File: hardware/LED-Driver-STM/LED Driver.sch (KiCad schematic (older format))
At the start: 3 parts, among them Q1 2N7002

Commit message: Finished Routing V1
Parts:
- D4: LCSC (none) -> C2286
- Q1: LCSC (none) -> C8545
- R9: LCSC (none) -> C25133
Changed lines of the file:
@@
 $Descr A4 11693 8268
 encoding utf-8
-Sheet 3 21
+Sheet 8 21
 Title ""
 Date ""
@@
 AR Path="/5F90BCB5/5F71D34C" Ref="R26"  Part="1"
 AR Path="/5F90BCB8/5F71D34C" Ref="R27"  Part="1"
-F 0 "R9" H 5368 3196 50  0000 L CNN
+F 0 "R14" H 5368 3196 50  0000 L CNN
 F 1 "75" H 5368 3105 50  0000 L CNN
 F 2 "Resistor_SMD:R_0402_1005Metric" H 5300 3150 50  0001 C CNN
 F 3 "~" H 5300 3150 50  0001 C CNN
 F 4 "C25133" H 5300 3150 50  0001 C CNN "LCSC Part #"
+F 5 "C25133" H 5300 3150 50  0001 C CNN "LCSC"
 	1    5300 3150
 	1    0    0    -1
@@
 AR Path="/5F90BCB5/5F71D352" Ref="D21"  Part="1"
 AR Path="/5F90BCB8/5F71D352" Ref="D22"  Part="1"
-F 0 "D4" V 5339 2683 50  0000 R CNN
+F 0 "D9" V 5339 2683 50  0000 R CNN
 F 1 "LED" V 5248 2683 50  0000 R CNN
 F 2 "LED_SMD:LED_0603_1608Metric_Castellated" H 5300 2800 50  0001 C CNN
 F 3 "~" H 5300 2800 50  0001 C CNN
 F 4 "C2286" H 5300 2800 50  0001 C CNN "LCSC Part #"
+F 5 "C2286" H 5300 2800 50  0001 C CNN "LCSC"
 	1    5300 2800
 	0    -1   -1   0
@@
 AR Path="/5F90BCB5/5F71EA4B" Ref="Q19"  Part="1"
 AR Path="/5F90BCB8/5F71EA4B" Ref="Q20"  Part="1"
-F 0 "Q2" H 5404 3596 50  0000 L CNN
+F 0 "Q7" H 5404 3596 50  0000 L CNN
 F 1 "2N7002" H 5404 3505 50  0000 L CNN
 F 2 "Package_TO_SOT_SMD:SOT-23" H 5400 3475 50  0001 L CIN
 F 3 "https://datasheet.lcsc.com/szlcsc/Changjiang-Electronics-Tech-CJ-2N7002_C8545.pdf" H 5200 3550 50  0001 L CNN
 F 4 "C8545" H 5200 3550 50  0001 C CNN "LCSC Part #"
+F 5 "C8545" H 5200 3550 50  0001 C CNN "LCSC"
 	1    5200 3550
 	1    0    0    -1

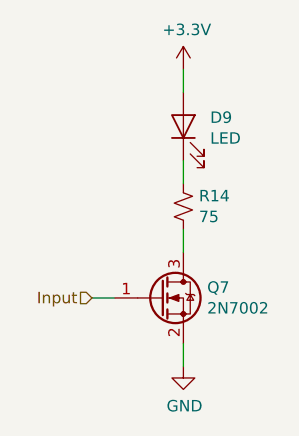
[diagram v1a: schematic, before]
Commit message: Latest board layout
This is the board that was purchased
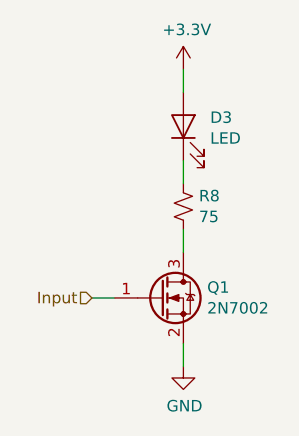
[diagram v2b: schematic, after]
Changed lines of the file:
@@
 $Descr A4 11693 8268
 encoding utf-8
-Sheet 8 21
+Sheet 2 21
 Title ""
 Date ""
@@
 AR Path="/5F90BCB5/5F71D34C" Ref="R26"  Part="1"
 AR Path="/5F90BCB8/5F71D34C" Ref="R27"  Part="1"
-F 0 "R14" H 5368 3196 50  0000 L CNN
+F 0 "R8" H 5368 3196 50  0000 L CNN
 F 1 "75" H 5368 3105 50  0000 L CNN
 F 2 "Resistor_SMD:R_0402_1005Metric" H 5300 3150 50  0001 C CNN
@@
 AR Path="/5F90BCB5/5F71D352" Ref="D21"  Part="1"
 AR Path="/5F90BCB8/5F71D352" Ref="D22"  Part="1"
-F 0 "D9" V 5339 2683 50  0000 R CNN
+F 0 "D3" V 5339 2683 50  0000 R CNN
 F 1 "LED" V 5248 2683 50  0000 R CNN
 F 2 "LED_SMD:LED_0603_1608Metric_Castellated" H 5300 2800 50  0001 C CNN
@@
 AR Path="/5F90BCB5/5F71EA4B" Ref="Q19"  Part="1"
 AR Path="/5F90BCB8/5F71EA4B" Ref="Q20"  Part="1"
-F 0 "Q7" H 5404 3596 50  0000 L CNN
+F 0 "Q1" H 5404 3596 50  0000 L CNN
 F 1 "2N7002" H 5404 3505 50  0000 L CNN
 F 2 "Package_TO_SOT_SMD:SOT-23" H 5400 3475 50  0001 L CIN
